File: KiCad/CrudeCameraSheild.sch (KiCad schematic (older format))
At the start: 284 parts, among them J1 GPIO, Q1 ALS-PT19, Q10 ALS-PT19, Q100 ALS-PT19, Q101 ALS-PT19, Q102 ALS-PT19, Q103 ALS-PT19, Q104 ALS-PT19, Q105 ALS-PT19, Q106 ALS-PT19, Q107 ALS-PT19, Q108 ALS-PT19, Q109 ALS-PT19, Q11 ALS-PT19, Q110 ALS-PT19, Q111 ALS-PT19, Q112 ALS-PT19, Q113 ALS-PT19, Q114 ALS-PT19, Q115 ALS-PT19, Q116 ALS-PT19, Q117 ALS-PT19, Q118 ALS-PT19, Q119 ALS-PT19, Q12 ALS-PT19, Q120 ALS-PT19, Q121 ALS-PT19, Q122 ALS-PT19, Q123 ALS-PT19, Q124 ALS-PT19, Q125 ALS-PT19, Q126 ALS-PT19, Q127 ALS-PT19, Q128 ALS-PT19, Q129 ALS-PT19, Q13 ALS-PT19, Q130 ALS-PT19, Q131 ALS-PT19, Q132 ALS-PT19, Q133 ALS-PT19, Q134 ALS-PT19, Q135 ALS-PT19, Q136 ALS-PT19, Q137 ALS-PT19, Q138 ALS-PT19, Q139 ALS-PT19, Q14 ALS-PT19, Q140 ALS-PT19, Q141 ALS-PT19, Q142 ALS-PT19, Q143 ALS-PT19, Q144 ALS-PT19, Q145 ALS-PT19, Q146 ALS-PT19, Q147 ALS-PT19, Q148 ALS-PT19, Q149 ALS-PT19, Q15 ALS-PT19, Q150 ALS-PT19, Q151 ALS-PT19, Q152 ALS-PT19, Q153 ALS-PT19, Q154 ALS-PT19, Q155 ALS-PT19, Q156 ALS-PT19, Q157 ALS-PT19, Q158 ALS-PT19, Q159 ALS-PT19, Q16 ALS-PT19, Q160 ALS-PT19, Q161 ALS-PT19, Q162 ALS-PT19, Q163 ALS-PT19, Q164 ALS-PT19, Q165 ALS-PT19, Q166 ALS-PT19, Q167 ALS-PT19, Q168 ALS-PT19, Q169 ALS-PT19, Q17 ALS-PT19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

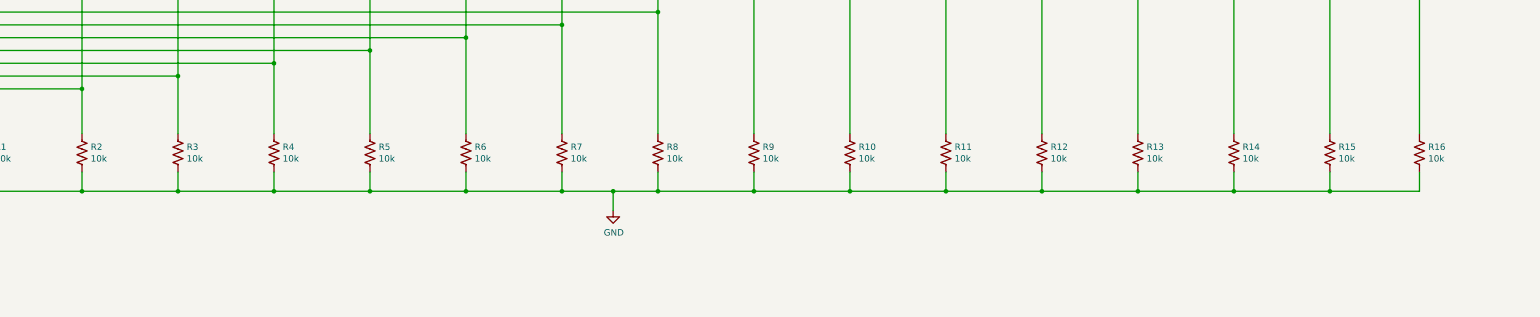
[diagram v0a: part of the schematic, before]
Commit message: Corrected spelling of sensor on silkscreen. Updated resistor values.
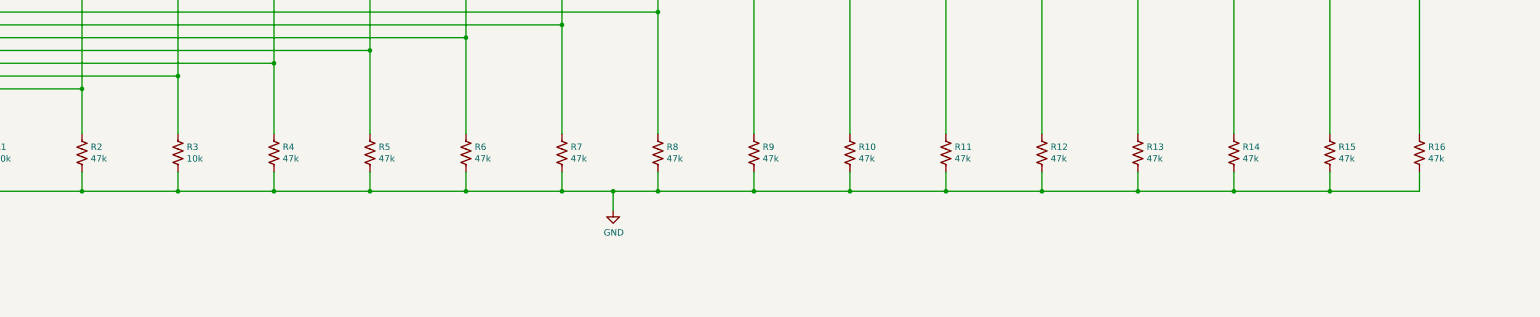
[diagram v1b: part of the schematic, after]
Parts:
- R10, R11, R12, R13, R14, R15, R16, R2, R4, R5, R6, R7, R8, R9: value 10k -> 47k
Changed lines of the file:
@@
 EESchema Schematic File Version 4
-LIBS:CrudeCameraSheild-cache
 EELAYER 30 0
 EELAYER END
@@
 encoding utf-8
 Sheet 1 1
-Title ""
-Date ""
-Rev ""
-Comp ""
+Title "Crude Camera Sensor"
+Date "2020-02-04"
+Rev "1.1"
+Comp "Northeastern Wireless Club"
 Comment1 ""
 Comment2 ""
@@
 P 26000 20200
 F 0 "R16" H 26068 20246 50  0000 L CNN
-F 1 "10k" H 26068 20155 50  0000 L CNN
+F 1 "47k" H 26068 20155 50  0000 L CNN
 F 2 "Resistor_SMD:R_1206_3216Metric_Pad1.42x1.75mm_HandSolder" V 26040 20190 50  0001 C CNN
 F 3 "~" H 26000 20200 50  0001 C CNN
@@
 P 25300 20200
 F 0 "R15" H 25368 20246 50  0000 L CNN
-F 1 "10k" H 25368 20155 50  0000 L CNN
+F 1 "47k" H 25368 20155 50  0000 L CNN
 F 2 "Resistor_SMD:R_1206_3216Metric_Pad1.42x1.75mm_HandSolder" V 25340 20190 50  0001 C CNN
 F 3 "~" H 25300 20200 50  0001 C CNN
@@
 P 24550 20200
 F 0 "R14" H 24618 20246 50  0000 L CNN
-F 1 "10k" H 24618 20155 50  0000 L CNN
+F 1 "47k" H 24618 20155 50  0000 L CNN
 F 2 "Resistor_SMD:R_1206_3216Metric_Pad1.42x1.75mm_HandSolder" V 24590 20190 50  0001 C CNN
 F 3 "~" H 24550 20200 50  0001 C CNN
@@
 P 23800 20200
 F 0 "R13" H 23868 20246 50  0000 L CNN
-F 1 "10k" H 23868 20155 50  0000 L CNN
+F 1 "47k" H 23868 20155 50  0000 L CNN
 F 2 "Resistor_SMD:R_1206_3216Metric_Pad1.42x1.75mm_HandSolder" V 23840 20190 50  0001 C CNN
 F 3 "~" H 23800 20200 50  0001 C CNN
@@
 P 23050 20200
 F 0 "R12" H 23118 20246 50  0000 L CNN
-F 1 "10k" H 23118 20155 50  0000 L CNN
+F 1 "47k" H 23118 20155 50  0000 L CNN
 F 2 "Resistor_SMD:R_1206_3216Metric_Pad1.42x1.75mm_HandSolder" V 23090 20190 50  0001 C CNN
 F 3 "~" H 23050 20200 50  0001 C CNN
@@
 P 22300 20200
 F 0 "R11" H 22368 20246 50  0000 L CNN
-F 1 "10k" H 22368 20155 50  0000 L CNN
+F 1 "47k" H 22368 20155 50  0000 L CNN
 F 2 "Resistor_SMD:R_1206_3216Metric_Pad1.42x1.75mm_HandSolder" V 22340 20190 50  0001 C CNN
 F 3 "~" H 22300 20200 50  0001 C CNN
@@
 P 21550 20200
 F 0 "R10" H 21618 20246 50  0000 L CNN
-F 1 "10k" H 21618 20155 50  0000 L CNN
+F 1 "47k" H 21618 20155 50  0000 L CNN
 F 2 "Resistor_SMD:R_1206_3216Metric_Pad1.42x1.75mm_HandSolder" V 21590 20190 50  0001 C CNN
 F 3 "~" H 21550 20200 50  0001 C CNN
@@
 P 20800 20200
 F 0 "R9" H 20868 20246 50  0000 L CNN
-F 1 "10k" H 20868 20155 50  0000 L CNN
+F 1 "47k" H 20868 20155 50  0000 L CNN
 F 2 "Resistor_SMD:R_1206_3216Metric_Pad1.42x1.75mm_HandSolder" V 20840 20190 50  0001 C CNN
 F 3 "~" H 20800 20200 50  0001 C CNN
@@
 P 20050 20200
 F 0 "R8" H 20118 20246 50  0000 L CNN
-F 1 "10k" H 20118 20155 50  0000 L CNN
+F 1 "47k" H 20118 20155 50  0000 L CNN
 F 2 "Resistor_SMD:R_1206_3216Metric_Pad1.42x1.75mm_HandSolder" V 20090 20190 50  0001 C CNN
 F 3 "~" H 20050 20200 50  0001 C CNN
@@
 P 19300 20200
 F 0 "R7" H 19368 20246 50  0000 L CNN
-F 1 "10k" H 19368 20155 50  0000 L CNN
+F 1 "47k" H 19368 20155 50  0000 L CNN
 F 2 "Resistor_SMD:R_1206_3216Metric_Pad1.42x1.75mm_HandSolder" V 19340 20190 50  0001 C CNN
 F 3 "~" H 19300 20200 50  0001 C CNN
@@
 P 18550 20200
 F 0 "R6" H 18618 20246 50  0000 L CNN
-F 1 "10k" H 18618 20155 50  0000 L CNN
+F 1 "47k" H 18618 20155 50  0000 L CNN
 F 2 "Resistor_SMD:R_1206_3216Metric_Pad1.42x1.75mm_HandSolder" V 18590 20190 50  0001 C CNN
 F 3 "~" H 18550 20200 50  0001 C CNN
@@
 P 17800 20200
 F 0 "R5" H 17868 20246 50  0000 L CNN
-F 1 "10k" H 17868 20155 50  0000 L CNN
+F 1 "47k" H 17868 20155 50  0000 L CNN
 F 2 "Resistor_SMD:R_1206_3216Metric_Pad1.42x1.75mm_HandSolder" V 17840 20190 50  0001 C CNN
 F 3 "~" H 17800 20200 50  0001 C CNN
@@
 P 17050 20200
 F 0 "R4" H 17118 20246 50  0000 L CNN
-F 1 "10k" H 17118 20155 50  0000 L CNN
+F 1 "47k" H 17118 20155 50  0000 L CNN
 F 2 "Resistor_SMD:R_1206_3216Metric_Pad1.42x1.75mm_HandSolder" V 17090 20190 50  0001 C CNN
 F 3 "~" H 17050 20200 50  0001 C CNN
@@
 	1    0    0    -1
 $EndComp
-$Comp
-L Device:R_US R2
-U 1 1 5F6679E0
-P 15550 20200
-F 0 "R2" H 15618 20246 50  0000 L CNN
-F 1 "10k" H 15618 20155 50  0000 L CNN
-F 2 "Resistor_SMD:R_1206_3216Metric_Pad1.42x1.75mm_HandSolder" V 15590 20190 50  0001 C CNN
-F 3 "~" H 15550 20200 50  0001 C CNN
-	1    15550 20200
-	1    0    0    -1
-$EndComp
-$Comp
-L Device:R_US R1
-U 1 1 5F6639C5
-P 14800 20200
-F 0 "R1" H 14868 20246 50  0000 L CNN
-F 1 "10k" H 14868 20155 50  0000 L CNN
-F 2 "Resistor_SMD:R_1206_3216Metric_Pad1.42x1.75mm_HandSolder" V 14840 20190 50  0001 C CNN
-F 3 "~" H 14800 20200 50  0001 C CNN
-	1    14800 20200
-	1    0    0    -1
-$EndComp
 Wire Wire Line
 	14800 20350 14800 20500
@@
 $EndComp
 NoConn ~ 12650 17700
+$Comp
+L Device:R_US R2
+U 1 1 5F6679E0
+P 15550 20200
+F 0 "R2" H 15618 20246 50  0000 L CNN
+F 1 "47k" H 15618 20155 50  0000 L CNN
+F 2 "Resistor_SMD:R_1206_3216Metric_Pad1.42x1.75mm_HandSolder" V 15590 20190 50  0001 C CNN
+F 3 "~" H 15550 20200 50  0001 C CNN
+	1    15550 20200
+	1    0    0    -1
+$EndComp
+$Comp
+L Device:R_US R1
+U 1 1 5F6639C5
+P 14800 20200
+F 0 "R1" H 14868 20246 50  0000 L CNN
+F 1 "10k" H 14868 20155 50  0000 L CNN
+F 2 "Resistor_SMD:R_1206_3216Metric_Pad1.42x1.75mm_HandSolder" V 14840 20190 50  0001 C CNN
+F 3 "~" H 14800 20200 50  0001 C CNN
+	1    14800 20200
+	1    0    0    -1
+$EndComp
 $EndSCHEMATC
